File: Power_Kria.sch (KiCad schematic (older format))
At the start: 68 parts, among them IC14 MP5016HGQH-Z, IC15 INA260AIPW, J10 PJ-202BH, J11 0022112022‎, Q13 DMN26D0UFB4-7, Q14 IRFHS8342TRPBF, Q15 DMN26D0UFB4-7, Q16 NDS331N, U17 MP8904, U18 MPM3810AGQB-Z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

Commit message: Update May --> See Update Note
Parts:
- removed C122, C130: 10uF, Capacitor_SMD:C_0402_1005Metric, symbol Device:C
- removed C128: 10000pF, Capacitor_SMD:C_0402_1005Metric, symbol Device:C
- removed D9: SD2114S040S8R0, ApotheoTech_CXP_Lib:SD2114S040S8RO, symbol ApotheoTech:SD2114S040S8R0
- removed J10: PJ-202BH, ApotheoTech_CXP_Lib:CUI_PJ-202B, symbol ApotheoTech:PJ-202B
- removed R105, R110: 10K, Resistor_SMD:R_0402_1005Metric, symbol Device:R
- removed R109: 20K, Resistor_SMD:R_0402_1005Metric, symbol Device:R
- removed U17: MP8904, ApotheoTech_CXP_Lib:MP8904DD, symbol ApotheoTech:MP8904
- added J10: MS12ANG03, ApotheoTech_CXP_Lib:MS12ANG03, symbol ApotheoTech:MS12ANG03
- added J2: PJ-063BH, ApotheoTech_CXP_Lib:CUI_PJ-063BH, symbol ApotheoTech:PJ-063BH
- added R37: 300k, Resistor_SMD:R_0402_1005Metric, symbol Device:R
- IC14: footprint MP5016HGQHZ -> ApotheoTech_CXP_Lib:MP5016HGQHZ
- R114: DNP (none) -> DNP
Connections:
- net 12V_IN_B4_LIMIT: now also J2.1, R37.2
- net GND: now also J10.3, J2.S1 (SHIELD), J2.S2 (SHIELD)
- net at R8.1: now also J2.2
- net MP5016_EN: now reaches IC14.9 (EN), R114.2
- net MP5016_EN: now also J10.2
- new net: J10.1, R37.1
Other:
- note added: "Plug detect will force board to an off state if no plug\nis currently in the 12V In jack.\nThis means we cannot have this tied here without a switch if we want to power via CoaXPress"
- note added: "Supply\nINA226 - 330uA typical supply\nSI5332 - 70mA (page 22/76)\nSI570 - 108mA (page 4/37)\nSI570 - 108mA (page 4/37)\nPIC - 350mA (max) page 738 of datasheet\n\nTotal powered devices - 636.33mA (max)\n\n\n\n"
- note removed: "12V in via CXP or Plug\nMust check via CXP how to properly power board via CXP\nQuestion: should place Diode on PG-202B to 12V In net?"
- note removed: "IGLOO 1V5 for Core Operation (RESET)"
- note removed: "Plug detect will force board to an off state if no plug\nis currently in the 12V In jack.\nThis means we cannot have this tied here without a switch"
- note removed: "Supply\nINA226 - 330uA typical supply\nSI5332 - 70mA (page 22/76)\nSI570 - 108mA (page 4/37)\nSI570 - 108mA (page 4/37)\nIGLOO Nano VCC0/1 - 5uA (page 24/136)\n\nTotal powered devices - 286mA\n\n\n\n"
- moved on the sheet: C124, R114, R8

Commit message: Pre-Production Push
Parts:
- C140, C151, C152: value 0.1uF -> DNP; DNP_Val (none) -> 0.1uF
- C143: value 0.1uF -> DNP; DNP_VAL (none) -> 0.1uF
- R114: value 300k -> DNP; DNP_Val (none) -> 300k
- R119: value 422 -> 0; PartNumber ERJ-2RKF4220X -> CRCW04020000Z0EDHP; Power 1/10W -> 1/5W; URL https://www.digikey.com/en/products/detail/ERJ-2RKF4220X/P4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 -> (none)
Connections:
- net ALERT_INA260 renamed HDA19_ALERT_INA260
- net HDA20_FAN renamed HDC09_FAN_PWM
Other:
- note added: "Max current Draw for SOM (all are max current into SOM)\n5V@4A for SOM (20W)\nHPA 1.2V@1A (1.2W)\nHDA, HDC 3.3V@1A (6.6W)\nHPC, HPB, HDB VADJ@1A (worst case 6W)\nSLVS-EC FRAMOS 3.8V@0.6A, 1.8V@0.6A (3.36W)\nMIPI Cameras (per 1 3.3V@0.5A) 1.65W (x2) (3.3W)\nDP power (3.3V@0.5A) 1.65W\nFMC 3V3 PWR (3.3V@3.1A) 10.23W\nFMC VADJ PWR(VADJ@4A) (worst case 8W)\n\nTotal \n60W for all peripherals on at sam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"
- note added: "Voltage limit (13.7V)\nCurrent Limit (8A)\n\nThus max power to board before shutdown is 96W"
- note removed: "Max current Draw for SOM (all are max current into SOM)\n5V@4A for SOM (20W)\nHPA, HPB 1.2V@1A (2.4W)\nHDA, HDB 3.3V@1A (6.6W)\nHPC, HDC 1.8V@1A (3.6W)\nIAS0 1.8V@0.2A, 1.2V@0.2A, 2.75V@0.2A (1.15W)\nSLVS-EC FRAMOS 3.8V@0.6A, 1.8V@0.6A (3.36W)\nMIPI Cameras (per 1 3.3V@0.5A) 1.65W (x4) (6.6W)\nDP power ?\n\nTotal (without DP)\n43.71W for all peripherals on at same time, with max power draw (Proba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"
- note removed: "Voltage limit (13.7V)\nCurrent Limit (5A)\n\nThus max power to board is 68.5W, nominal is 12V@5A (60W)"
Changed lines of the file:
@@
 Connection ~ 12655 3275
 Text HLabel 12305 3275 0    50   Input ~ 0
-HDA20_FAN
+HDC09_FAN_PWM
 Wire Wire Line
 	13455 2475 13455 2325
@@
 AR Path="/6374AD8D/61C5F957" Ref="C151"  Part="1"
 F 0 "C151" H 15545 2565 50  0000 C CNN
-F 1 "0.1uF" H 15485 2630 50  0000 C CNN
+F 1 "DNP" H 15485 2630 50  0000 C CNN
 F 2 "Capacitor_SMD:C_0402_1005Metric" H 15743 2475 50  0001 C CNN
 F 3 "~" H 15705 2625 50  0001 C CNN
@@
 F 7 "X5R" H 15705 2625 50  0001 C CNN "Temp_Val"
 F 8 "https://www.digikey.com/en/products/detail/TMK105BJ104KVHF/587-3808-1-ND/4811278?itemSeq=375666509" V 15705 2625 50  0001 C CNN "URL"
-F 9 "DNP" H 15705 2625 79  0000 C CNB "DNP"
+F 9 "DNP" H 15710 2735 79  0000 C CNB "DNP"
+F 10 "0.1uF" H 15705 2625 50  0001 C CNN "DNP_Val"
 	1    15705 2625
 	-1   0    0    1
@@
 AR Path="/6374AD8D/61C64F04" Ref="C152"  Part="1"
 F 0 "C152" H 16045 2565 50  0000 C CNN
-F 1 "0.1uF" H 15985 2630 50  0000 C CNN
+F 1 "DNP" H 15985 2630 50  0000 C CNN
 F 2 "Capacitor_SMD:C_0402_1005Metric" H 16243 2475 50  0001 C CNN
 F 3 "~" H 16205 2625 50  0001 C CNN
@@
 F 7 "X5R" H 16205 2625 50  0001 C CNN "Temp_Val"
 F 8 "https://www.digikey.com/en/products/detail/TMK105BJ104KVHF/587-3808-1-ND/4811278?itemSeq=375666509" V 16205 2625 50  0001 C CNN "URL"
-F 9 "DNP" H 16205 2625 79  0000 C CNB "DNP"
+F 9 "DNP" H 16200 2750 79  0000 C CNB "DNP"
+F 10 "0.1uF" H 16205 2625 50  0001 C CNN "DNP_Val"
 	1    16205 2625
 	-1   0    0    1
@@
 AR Path="/6374AD8D/615B4E5D" Ref="R114"  Part="1"
 F 0 "R114" H 6135 3045 50  0000 L CNN
-F 1 "300k" H 6130 2980 50  0000 L CNN
+F 1 "DNP" H 6130 2980 50  0000 L CNN
 F 2 "Resistor_SMD:R_0402_1005Metric" V 5980 3050 50  0001 C CNN
 F 3 "~" H 6050 3050 50  0001 C CNN
@@
 F 7 "https://www.digikey.com/en/products/detail/ERJ-2RKF3003X/P300KLCT-ND/1746669?itemSeq=376404154" H 6050 3050 50  0001 C CNN "URL"
 F 8 "DNP" H 6050 3050 79  0000 C CIB "DNP"
+F 9 "300k" H 6050 3050 50  0001 C CNN "DNP_Val"
 	1    6050 3050
 	1    0    0    -1
@@
 AR Path="/6374AD8D/616137F5" Ref="C143"  Part="1"
 F 0 "C143" H 9440 3565 50  0000 C CNN
-F 1 "0.1uF" H 9380 3630 50  0000 C CNN
+F 1 "DNP" H 9380 3630 50  0000 C CNN
 F 2 "Capacitor_SMD:C_0402_1005Metric" H 9638 3475 50  0001 C CNN
 F 3 "~" H 9600 3625 50  0001 C CNN
@@
 F 7 "X5R" H 9600 3625 50  0001 C CNN "Temp_Val"
 F 8 "https://www.digikey.com/en/products/detail/TMK105BJ104KVHF/587-3808-1-ND/4811278?itemSeq=375666509" V 9600 3625 50  0001 C CNN "URL"
-F 9 "DNP" H 9600 3625 79  0000 C CNB "DNP"
+F 9 "DNP" H 9595 3770 79  0000 C CNB "DNP"
+F 10 "0.1uF" H 9600 3625 50  0001 C CNN "DNP_VAL"
 	1    9600 3625
 	-1   0    0    1
@@
 AR Path="/6314F719/6162F215" Ref="R?"  Part="1"
 AR Path="/6374AD8D/6162F215" Ref="R119"  Part="1"
-F 0 "R119" H 8885 3575 50  0000 L CNN
-F 1 "422" H 8800 3640 50  0000 L CNN
+F 0 "R119" H 8755 3565 50  0000 L CNN
+F 1 "0" H 8800 3640 50  0000 L CNN
 F 2 "Resistor_SMD:R_0402_1005Metric" V 8980 3625 50  0001 C CNN
 F 3 "~" H 9050 3625 50  0001 C CNN
 F 4 "1%" H 8875 3705 50  0000 L CNN "Tolerance"
-F 5 "1/10W" H 9050 3625 50  0001 C CNN "Power"
-F 6 "ERJ-2RKF4220X" H 9050 3625 50  0001 C CNN "PartNumber"
-F 7 "https://www.digikey.com/en/products/detail/ERJ-2RKF4220X/P422LCT-ND/194400?itemSeq=376477738" H 9050 3625 50  0001 C CNN "URL"
+F 5 "1/5W" H 9050 3625 50  0001 C CNN "Power"
+F 6 "CRCW04020000Z0EDHP" H 9050 3625 50  0001 C CNN "PartNumber"
+F 7 "" H 9050 3625 50  0001 C CNN "URL"
 	1    9050 3625
 	-1   0    0    1
@@
 AR Path="/6374AD8D/6164E358" Ref="C140"  Part="1"
 F 0 "C140" H 8490 3565 50  0000 C CNN
-F 1 "0.1uF" H 8430 3630 50  0000 C CNN
+F 1 "DNP" H 8430 3630 50  0000 C CNN
 F 2 "Capacitor_SMD:C_0402_1005Metric" H 8688 3475 50  0001 C CNN
 F 3 "~" H 8650 3625 50  0001 C CNN
@@
 F 7 "X5R" H 8650 3625 50  0001 C CNN "Temp_Val"
 F 8 "https://www.digikey.com/en/products/detail/TMK105BJ104KVHF/587-3808-1-ND/4811278?itemSeq=375666509" V 8650 3625 50  0001 C CNN "URL"
-F 9 "DNP" H 8650 3625 79  0000 C CNB "DNP"
+F 9 "DNP" H 8650 3755 79  0000 C CNB "DNP"
+F 10 "0.1uF" H 8650 3625 50  0001 C CNN "DNP_Val"
 	1    8650 3625
 	-1   0    0    1
@@
 Wire Wire Line
 	13455 2875 14205 2875
-Text Notes 7175 5755 0    50   ~ 0
+Text Notes 6855 5715 0    50   ~ 0
 12A for all board (gives us 60W)
-Text Notes 6695 5560 0    50   ~ 0
-Max current Draw for SOM (all are max current into SOM)\n5V@4A for SOM (20W)\nHPA, HPB 1.2V@1A (2.4W)\nHDA, HDB 3.3V@1A (6.6W)\nHPC, HDC 1.8V@1A (3.6W)\nIAS0 1.8V@0.2A, 1.2V@0.2A, 2.75V@0.2A (1.15W)\nSLVS-EC FRAMOS 3.8V@0.6A, 1.8V@0.6A (3.36W)\nMIPI Cameras (per 1 3.3V@0.5A) 1.65W (x4) (6.6W)\nDP power ?\n\nTotal (without DP)\n43.71W for all peripherals on at same time, with max power draw (Probably not ever going to happen)
+Text Notes 6845 5605 0    50   ~ 0
+Max current Draw for SOM (all are max current into SOM)\n5V@4A for SOM (20W)\nHPA           1.2V@1A (1.2W)\nHDA, HDC 3.3V@1A (6.6W)\nHPC, HPB, HDB VADJ@1A (worst case 6W)\nSLVS-EC FRAMOS 3.8V@0.6A, 1.8V@0.6A (3.36W)\nMIPI Cameras (per 1 3.3V@0.5A) 1.65W (x2) (3.3W)\nDP power (3.3V@0.5A) 1.65W\nFMC 3V3 PWR (3.3V@3.1A) 10.23W\nFMC VADJ PWR(VADJ@4A) (worst case 8W)\n\nTotal \n60W for all peripherals on at same time, with max power draw (Probably not ever going to happen)
 Text Notes 1125 2490 0    50   ~ 0
 PJ-202BH is rated for 5A so total of 60W to board
@@
 	2225 3620 2675 3620
 Text Notes 6955 4085 0    50   ~ 0
-Voltage limit (13.7V)\nCurrent Limit (5A)\n\nThus max power to board is 68.5W, nominal is 12V@5A (60W)
+Voltage limit (13.7V)\nCurrent Limit (8A)\n\nThus max power to board before shutdown is 96W
 $Comp
 L power:PWR_FLAG #FLG020
@@
 	3350 6400 3200 6400
 Text HLabel 15150 6400 2    50   Output ~ 0
-ALERT_INA260
+HDA19_ALERT_INA260
 $Comp
 L Device:R R?

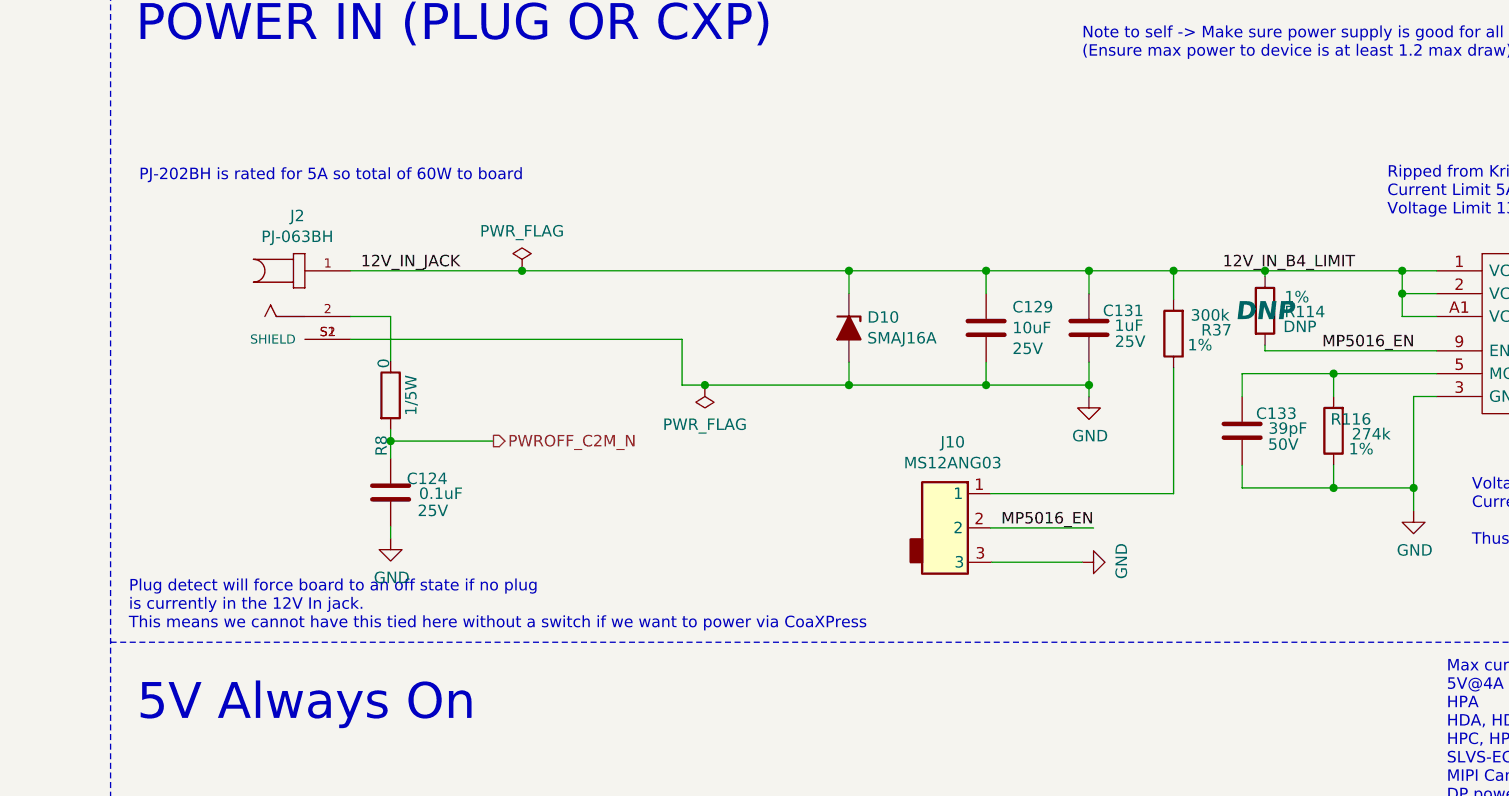
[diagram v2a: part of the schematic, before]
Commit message: Update to Kicad 7
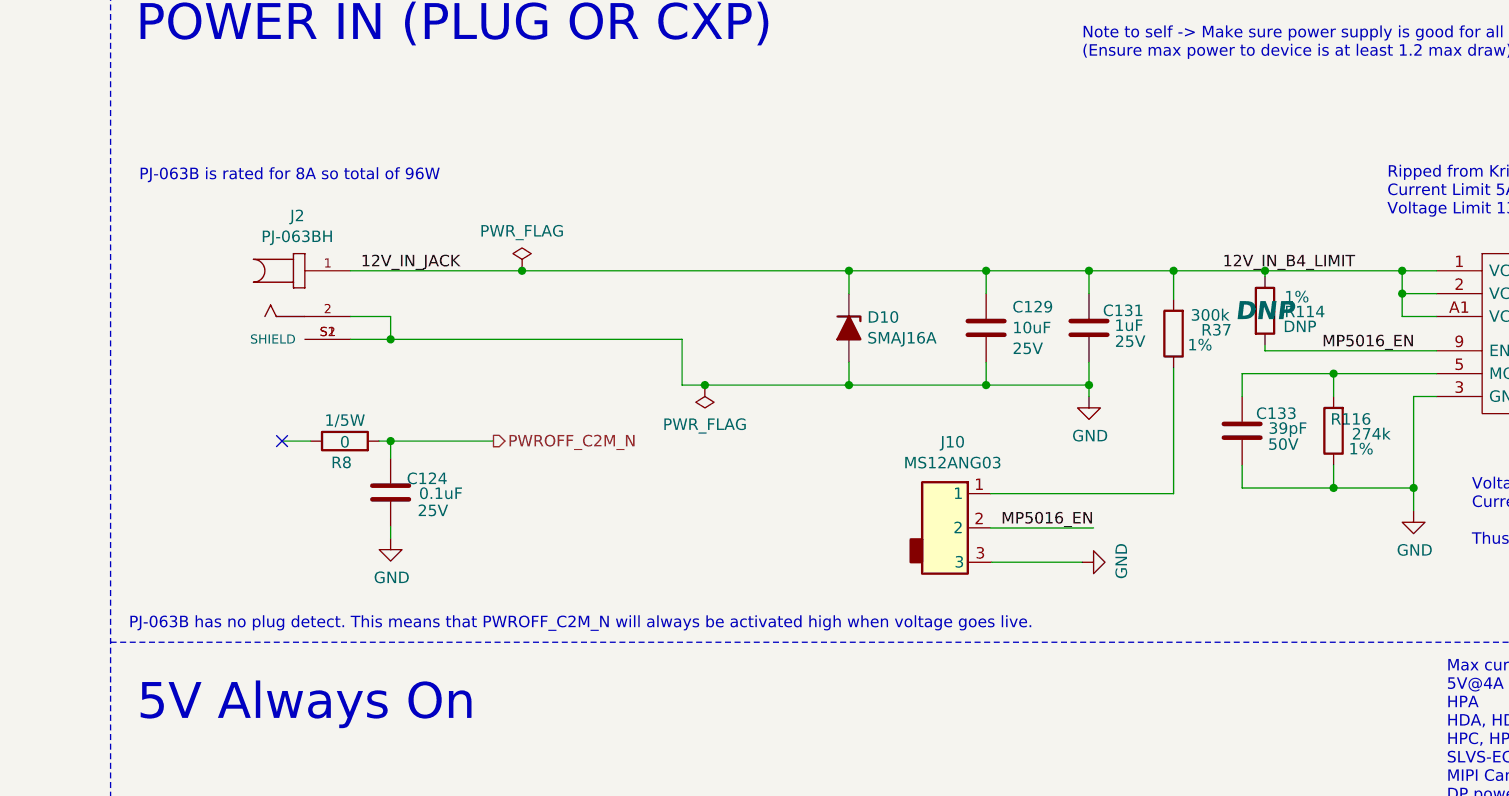
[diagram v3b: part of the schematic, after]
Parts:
- L14: PartNumber XAL5030-122ME -> XEL5030-122ME
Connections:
- net GND: now also J2.2
- net at R8.1: no longer J2.2
- no-connect marks 0 -> 1
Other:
- note added: "PJ-063B has no plug detect. This means that PWROFF_C2M_N will always be activated high when voltage goes live."
- note added: "PJ-063B is rated for 8A so total of 96W"
- note removed: "PJ-202BH is rated for 5A so total of 60W to board"
- note removed: "Plug detect will force board to an off state if no plug\nis currently in the 12V In jack.\nThis means we cannot have this tied here without a switch if we want to power via CoaXPress"
- moved on the sheet: R8
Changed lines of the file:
@@
 F 2 "ApotheoTech_CXP_Lib:XAL5030-122ME" H 6750 6000 50  0001 C CNN
 F 3 "~" H 6750 6000 50  0001 C CNN
-F 4 "XAL5030-122ME " V 6750 6000 50  0001 C CNN "PartNumber"
+F 4 "XEL5030-122ME " V 6750 6000 50  0001 C CNN "PartNumber"
 	1    6750 6000
 	0    -1   -1   0
@@
 	3500 3375 3600 3375
 Wire Wire Line
-	2050 3175 3500 3175
+	2050 3175 2225 3175
 Wire Wire Line
 	2050 2875 2800 2875
 Connection ~ 2800 2875
 Text Notes 1080 4450 0    50   ~ 0
-Plug detect will force board to an off state if no plug\nis currently in the 12V In jack.\nThis means we cannot have this tied here without a switch if we want to power via CoaXPress
+PJ-063B has no plug detect. This means that PWROFF_C2M_N will always be activated high when voltage goes live.
 Text Notes 1780 7920 0    50   ~ 0
 Pull up resistor with turn on MOSFET\n(pulls up PWROFF_C2M_N to high, to start SOM)
@@
 Max current Draw for SOM (all are max current into SOM)\n5V@4A for SOM (20W)\nHPA           1.2V@1A (1.2W)\nHDA, HDC 3.3V@1A (6.6W)\nHPC, HPB, HDB VADJ@1A (worst case 6W)\nSLVS-EC FRAMOS 3.8V@0.6A, 1.8V@0.6A (3.36W)\nMIPI Cameras (per 1 3.3V@0.5A) 1.65W (x2) (3.3W)\nDP power (3.3V@0.5A) 1.65W\nFMC 3V3 PWR (3.3V@3.1A) 10.23W\nFMC VADJ PWR(VADJ@4A) (worst case 8W)\n\nTotal \n60W for all peripherals on at same time, with max power draw (Probably not ever going to happen)
 Text Notes 1125 2490 0    50   ~ 0
-PJ-202BH is rated for 5A so total of 60W to board
+PJ-063B is rated for 8A so total of 96W
 Wire Wire Line
 	2225 3620 2225 3695
@@
 L Device:R R?
 U 1 1 61A10DB5
-P 2225 3420
+P 2025 3620
 AR Path="/5F71E4A6/61A10DB5" Ref="R?"  Part="1"
 AR Path="/5F71E87D/61A10DB5" Ref="R?"  Part="1"
 AR Path="/6374AD8D/61A10DB5" Ref="R8"  Part="1"
-F 0 "R8" V 2185 3200 50  0000 C CNN
-F 1 "0" V 2195 3560 50  0000 C CNN
-F 2 "Resistor_SMD:R_0402_1005Metric" V 2155 3420 50  0001 C CNN
-F 3 "~" H 2225 3420 50  0001 C CNN
-F 4 "CRCW04020000Z0EDHP" V 2225 3420 50  0001 C CNN "PartNumber"
-F 5 "1/5W" V 2315 3420 50  0000 C CNN "Power"
-F 6 "https://www.digikey.com/product-detail/en/vishay-dale/CRCW04020000Z0EDHP/541-0-0YBCT-ND/2223008" V 2225 3420 50  0001 C CNN "URL"
-	1    2225 3420
-	1    0    0    -1
-$EndComp
-Wire Wire Line
-	2225 3570 2225 3620
-Connection ~ 2225 3620
+F 0 "R8" V 1930 3635 50  0000 C CNN
+F 1 "0" V 2020 3620 50  0000 C CNN
+F 2 "Resistor_SMD:R_0402_1005Metric" V 1955 3620 50  0001 C CNN
+F 3 "~" H 2025 3620 50  0001 C CNN
+F 4 "CRCW04020000Z0EDHP" V 2025 3620 50  0001 C CNN "PartNumber"
+F 5 "1/5W" V 2115 3620 50  0000 C CNN "Power"
+F 6 "https://www.digikey.com/product-detail/en/vishay-dale/CRCW04020000Z0EDHP/541-0-0YBCT-ND/2223008" V 2025 3620 50  0001 C CNN "URL"
+	1    2025 3620
+	0    -1   -1   0
+$EndComp
+Wire Wire Line
+	2175 3620 2225 3620
 Text GLabel 12950 6525 0    50   Input ~ 0
 I2C_SCL_PS_SIDE
@@
 Wire Wire Line
 	3500 3175 3500 3375
-Wire Wire Line
-	2225 3270 2225 3075
 Wire Wire Line
 	2225 3075 2050 3075
@@
 Wire Wire Line
 	6050 2875 6650 2875
+Connection ~ 2225 3620
+Wire Wire Line
+	1875 3620 1750 3620
+NoConn ~ 1750 3620
+Wire Wire Line
+	2225 3075 2225 3175
+Connection ~ 2225 3175
+Wire Wire Line
+	2225 3175 3500 3175
 $EndSCHEMATC
